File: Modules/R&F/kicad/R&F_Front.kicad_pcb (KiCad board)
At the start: 2 copper layers, 14.5 x 108.6 mm, 21 parts

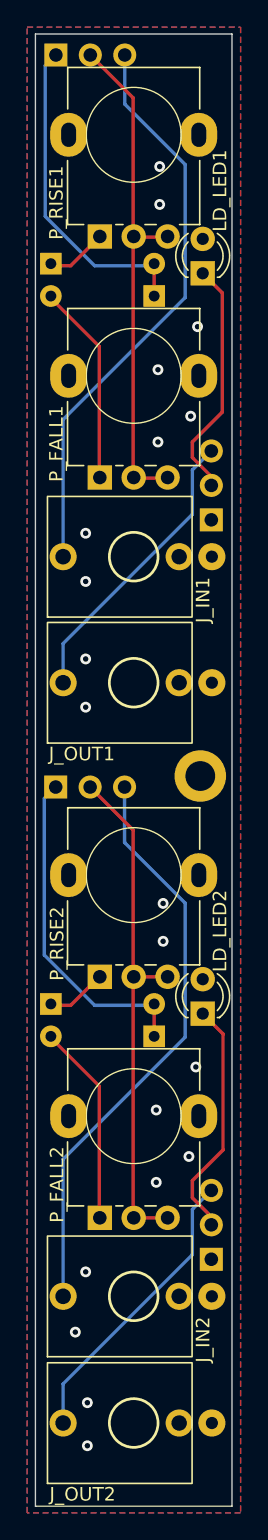
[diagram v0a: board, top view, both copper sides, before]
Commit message: Add Interactive BOMs, resave all PCBs, move VU to THT.
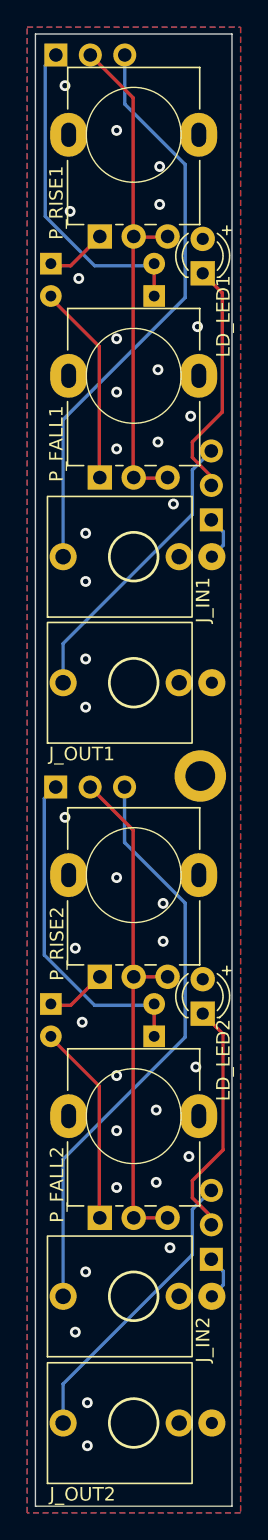
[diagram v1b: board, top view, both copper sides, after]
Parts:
- removed the G*** at (38.4, 137.4)
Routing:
- net GND: track 0.00 -> 6.89 mm, vias 20 -> 36
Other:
- board text added: "R&F v1.1"
- board text removed: "R&F v1.0"
